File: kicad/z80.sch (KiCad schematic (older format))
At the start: 18 parts, among them J3 Conn_02x20_Odd_Even, U1 Z80CPU, U23 74AC273, U3 SST39SF010, U4 74AHC32, U5 AS6C1008-55PCN, U6 74HC154, U9 74AHC02, X1 ACH10MHZ

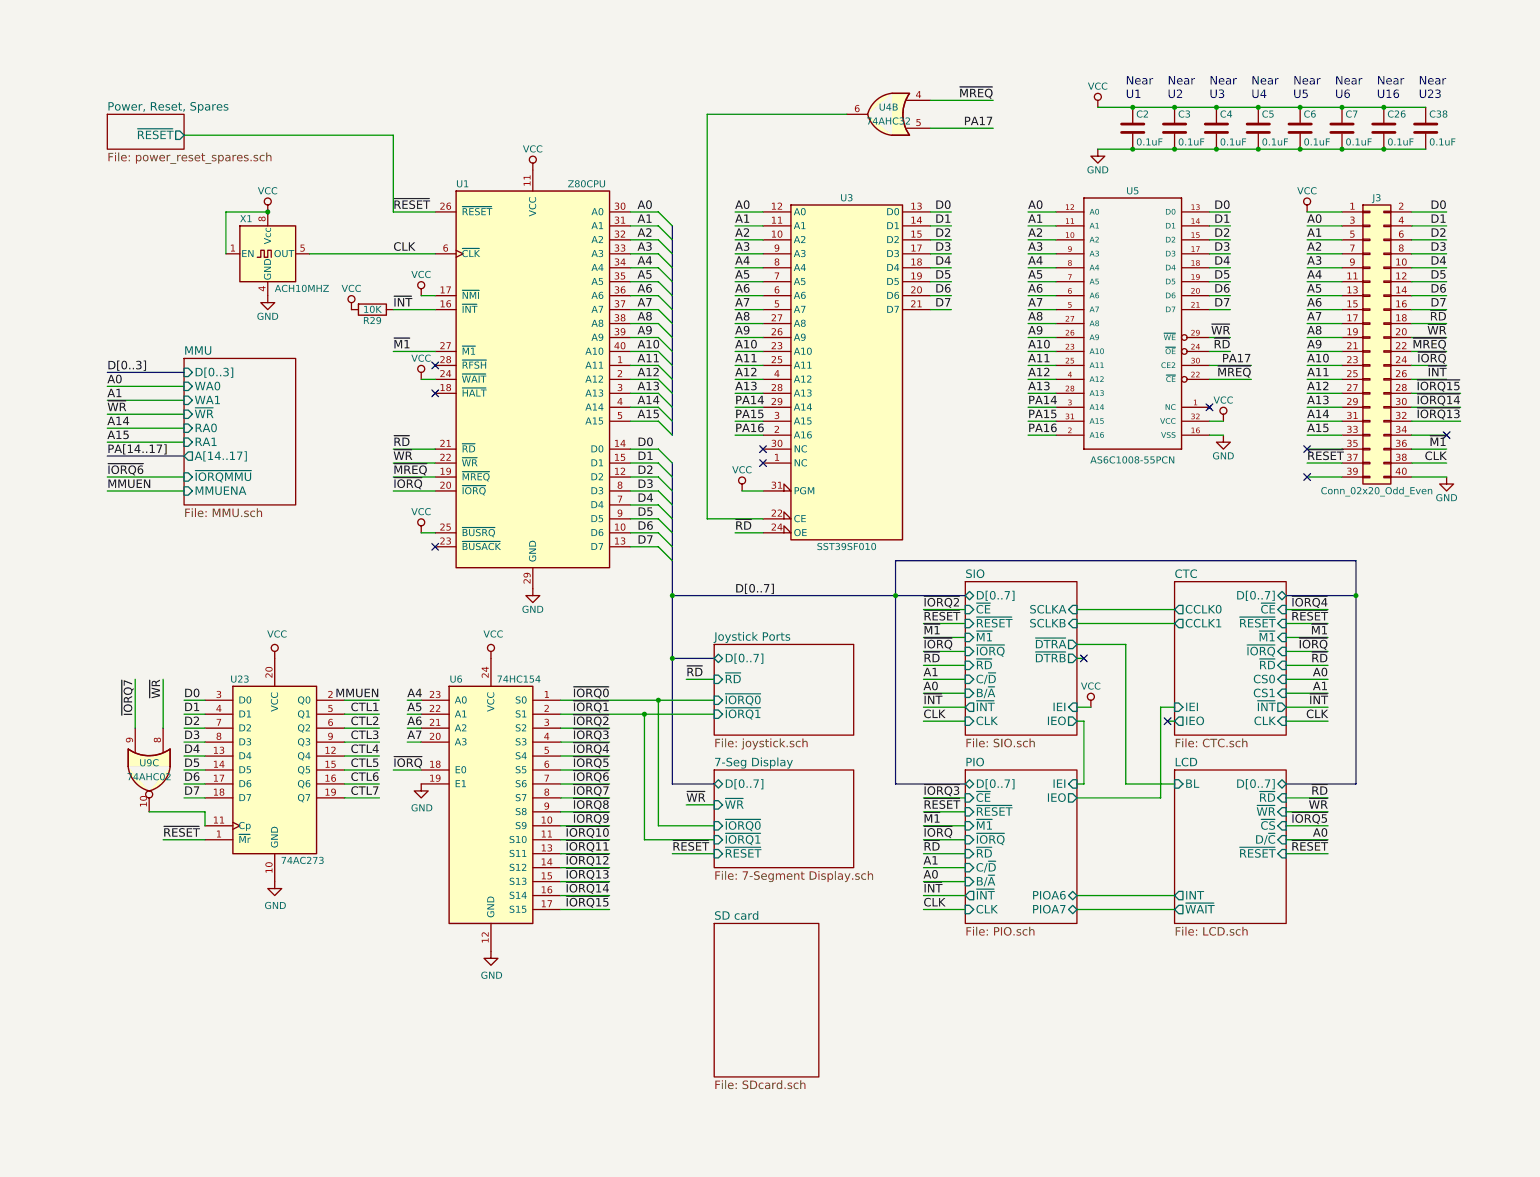
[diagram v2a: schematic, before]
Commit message: SDcard interface mostly complete.
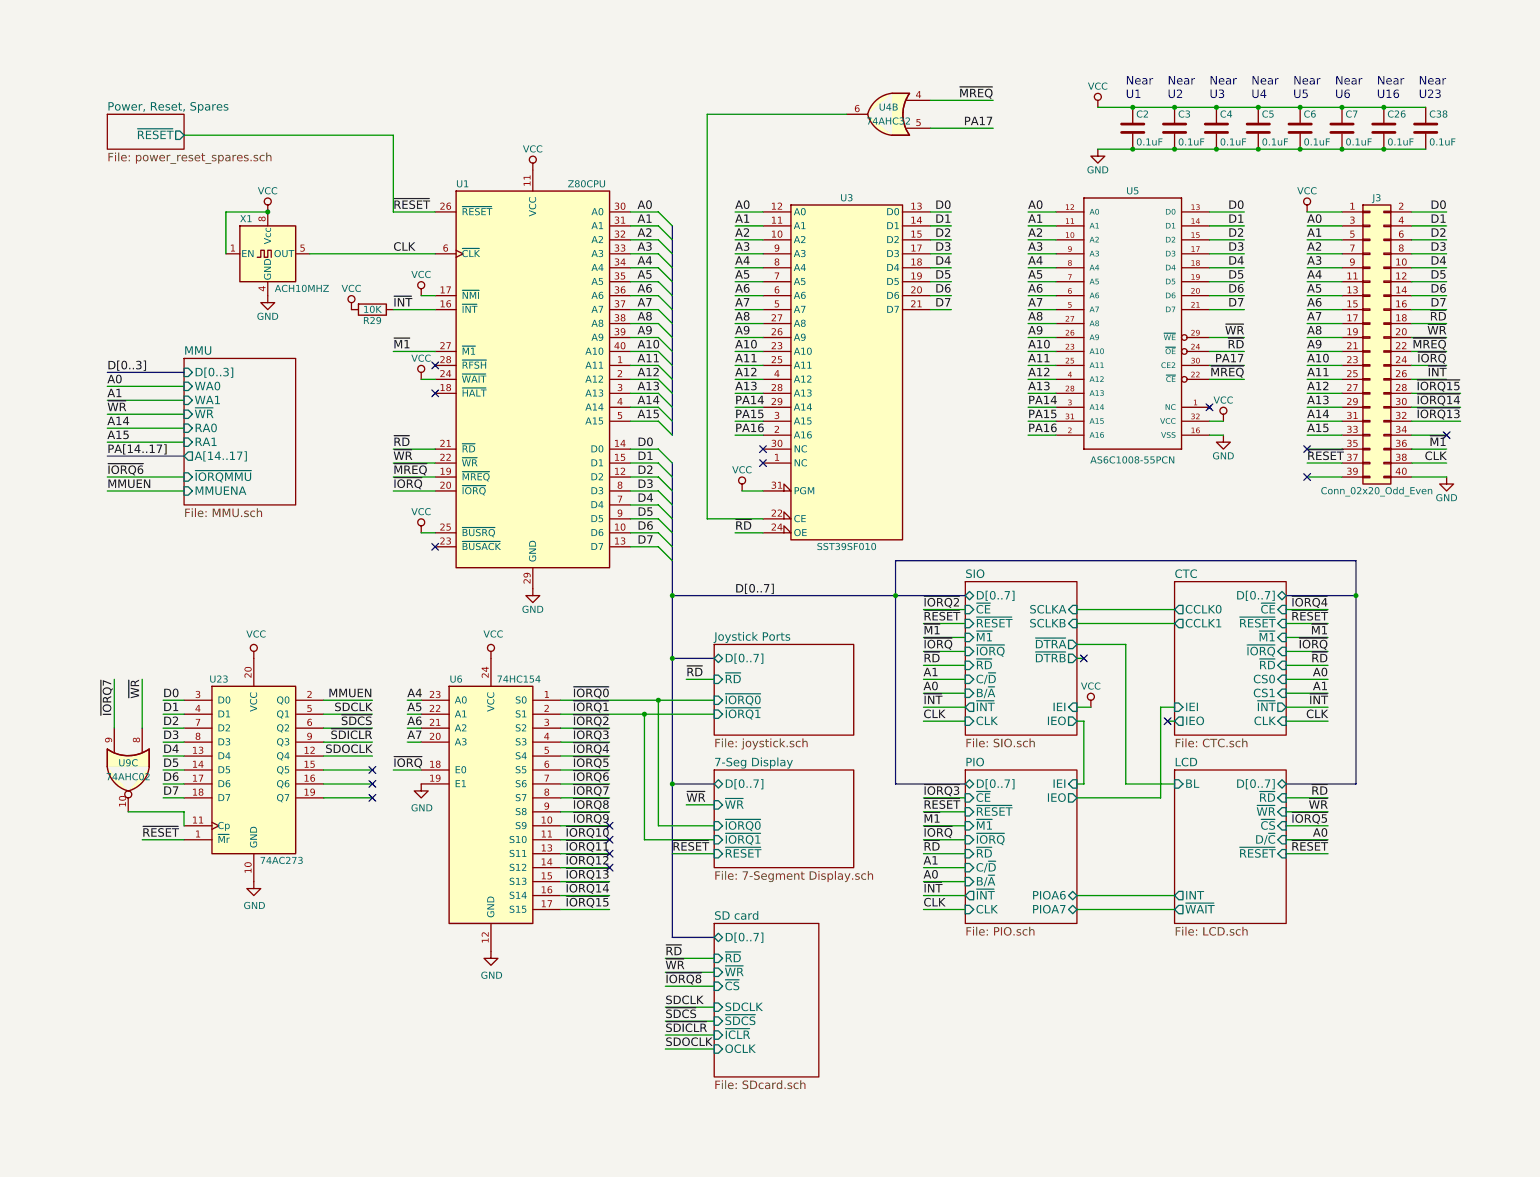
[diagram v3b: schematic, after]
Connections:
- net CTL1 renamed SDCLK
- net CTL2 renamed ~SDCS
- net CTL3 renamed ~SDICLR
- net CTL4 renamed SDOCLK
- net CTL5: no longer names the net of U23.15 (Q5)
- net CTL6: no longer names the net of U23.16 (Q6)
- net CTL7: no longer names the net of U23.19 (Q7)
- no-connect marks 11 -> 18
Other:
- moved on the sheet: U23, U9C
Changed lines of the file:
@@
 	1    0    0    -1
 $EndComp
-Text Label 8750 1550 2    60   ~ 0
+Text Label 8850 1550 2    60   ~ 0
 D0
-Text Label 8750 1650 2    60   ~ 0
+Text Label 8850 1650 2    60   ~ 0
 D1
-Text Label 8750 1750 2    60   ~ 0
+Text Label 8850 1750 2    60   ~ 0
 D2
-Text Label 8750 1850 2    60   ~ 0
+Text Label 8850 1850 2    60   ~ 0
 D3
-Text Label 8750 1950 2    60   ~ 0
+Text Label 8850 1950 2    60   ~ 0
 D4
-Text Label 8750 2050 2    60   ~ 0
+Text Label 8850 2050 2    60   ~ 0
 D5
-Text Label 8750 2150 2    60   ~ 0
+Text Label 8850 2150 2    60   ~ 0
 D6
-Text Label 8750 2250 2    60   ~ 0
+Text Label 8850 2250 2    60   ~ 0
 D7
 Text Label 7300 1550 0    60   ~ 0
@@
 Text Label 5200 3050 0    60   ~ 0
 PA15
-Text Label 8750 2450 2    60   ~ 0
+Text Label 8850 2450 2    60   ~ 0
 ~WR
-Text Label 8750 2550 2    60   ~ 0
+Text Label 8850 2550 2    60   ~ 0
 ~RD
 NoConn ~ 8600 2950
@@
 Text Notes 9200 750  0    60   ~ 0
 Near\nU5
-Text Label 8900 2750 2    60   ~ 0
+Text Label 8850 2750 2    60   ~ 0
 ~MREQ
 Text Label 2750 5550 0    60   ~ 0
@@
 Text Label 700  3450 0    60   ~ 0
 ~IORQ6
-Text Label 900  4900 3    60   ~ 0
+Text Label 750  4900 3    60   ~ 0
 ~IORQ7
 Text Label 700  3300 0    60   ~ 0
@@
 	7500 3150 7300 3150
 Wire Wire Line
-	8600 1550 8750 1550
-Wire Wire Line
-	8600 1650 8750 1650
-Wire Wire Line
-	8600 1750 8750 1750
-Wire Wire Line
-	8600 1850 8750 1850
-Wire Wire Line
-	8600 1950 8750 1950
-Wire Wire Line
-	8600 2050 8750 2050
-Wire Wire Line
-	8600 2150 8750 2150
-Wire Wire Line
-	8600 2250 8750 2250
-Wire Wire Line
 	7500 1550 7300 1550
 Wire Wire Line
@@
 Wire Wire Line
 	5400 3050 5200 3050
-Wire Wire Line
-	8600 2550 8750 2550
-Wire Wire Line
-	8600 2450 8750 2450
 Connection ~ 8950 800
 Connection ~ 8950 1100
-Wire Wire Line
-	8600 2750 8900 2750
-Wire Wire Line
-	8600 2650 8900 2650
 Connection ~ 9250 800
 Connection ~ 9250 1100
@@
 	700  3450 1250 3450
 Wire Wire Line
-	900  4900 900  5250
+	750  4900 750  5250
 Wire Bus Line
 	1250 2700 700  2700
@@
 Text Label 7300 3150 0    60   ~ 0
 PA16
-Text Label 8900 2650 2    60   ~ 0
+Text Label 8850 2650 2    60   ~ 0
 PA17
 Text Label 7050 950  2    60   ~ 0
@@
 F0 "SD card" 60
 F1 "SDcard.sch" 60
+F2 "D[0..7]" B L 5050 6750 60
+F3 "~RD" I L 5050 6900 60
+F4 "~WR" I L 5050 7000 60
+F5 "~CS" I L 5050 7100 60
+F6 "SDCLK" I L 5050 7250 60
+F7 "~SDCS" I L 5050 7350 60
+F8 "OCLK" I L 5050 7550 60
+F9 "~ICLR" I L 5050 7450 60
 $EndSheet
 $Comp
 L 74xx:74LS273 U23
 U 1 1 5C3D0091
-P 1900 5550
-F 0 "U23" H 1650 6200 50  0000 C CNN
-F 1 "74AC273" H 2100 4900 50  0000 C CNN
-F 2 "" H 1900 5550 50  0001 C CNN
-F 3 "http://www.ti.com/lit/gpn/sn74LS273" H 1900 5550 50  0001 C CNN
-	1    1900 5550
-	1    0    0    -1
-$EndComp
-Text Label 1100 6050 0    60   ~ 0
+P 1750 5550
+F 0 "U23" H 1500 6200 50  0000 C CNN
+F 1 "74AC273" H 1950 4900 50  0000 C CNN
+F 2 "" H 1750 5550 50  0001 C CNN
+F 3 "http://www.ti.com/lit/gpn/sn74LS273" H 1750 5550 50  0001 C CNN
+	1    1750 5550
+	1    0    0    -1
+$EndComp
+Text Label 950  6050 0    60   ~ 0
 ~RESET
-Text Label 1250 5050 0    60   ~ 0
+Text Label 1100 5050 0    60   ~ 0
 D0
-Text Label 1250 5150 0    60   ~ 0
+Text Label 1100 5150 0    60   ~ 0
 D1
-Text Label 1250 5250 0    60   ~ 0
+Text Label 1100 5250 0    60   ~ 0
 D2
-Text Label 1250 5350 0    60   ~ 0
+Text Label 1100 5350 0    60   ~ 0
 D3
-Text Label 1250 5450 0    60   ~ 0
+Text Label 1100 5450 0    60   ~ 0
 D4
-Text Label 1250 5550 0    60   ~ 0
+Text Label 1100 5550 0    60   ~ 0
 D5
-Text Label 1250 5650 0    60   ~ 0
+Text Label 1100 5650 0    60   ~ 0
 D6
-Text Label 1250 5750 0    60   ~ 0
+Text Label 1100 5750 0    60   ~ 0
 D7
 Wire Wire Line
-	1400 5050 1250 5050
-Wire Wire Line
-	1400 5150 1250 5150
-Wire Wire Line
-	1400 5250 1250 5250
-Wire Wire Line
-	1400 5350 1250 5350
-Wire Wire Line
-	1400 5450 1250 5450
-Wire Wire Line
-	1400 5550 1250 5550
-Wire Wire Line
-	1400 5650 1250 5650
-Wire Wire Line
-	1400 5750 1250 5750
-Wire Wire Line
-	1100 6050 1400 6050
-Wire Wire Line
-	2400 5050 2650 5050
-Wire Wire Line
-	2400 5150 2650 5150
-Wire Wire Line
-	2400 5250 2650 5250
-Wire Wire Line
-	2400 5350 2650 5350
-Wire Wire Line
-	2400 5450 2650 5450
-Wire Wire Line
-	2400 5550 2650 5550
-Wire Wire Line
-	2400 5650 2650 5650
-Wire Wire Line
-	2400 5750 2650 5750
-Text Label 2650 5050 2    60   ~ 0
+	1250 5050 1100 5050
+Wire Wire Line
+	1250 5150 1100 5150
+Wire Wire Line
+	1250 5250 1100 5250
+Wire Wire Line
+	1250 5350 1100 5350
+Wire Wire Line
+	1250 5450 1100 5450
+Wire Wire Line
+	1250 5550 1100 5550
+Wire Wire Line
+	1250 5650 1100 5650
+Wire Wire Line
+	1250 5750 1100 5750
+Wire Wire Line
+	950  6050 1250 6050
+Text Label 2600 5050 2    60   ~ 0
 MMUEN
-Text Label 2650 5150 2    60   ~ 0
-CTL1
-Text Label 2650 5250 2    60   ~ 0
-CTL2
-Text Label 2650 5350 2    60   ~ 0
-CTL3
-Text Label 2650 5450 2    60   ~ 0
-CTL4
-Text Label 2650 5550 2    60   ~ 0
-CTL5
-Text Label 2650 5650 2    60   ~ 0
-CTL6
-Text Label 2650 5750 2    60   ~ 0
-CTL7
+Text Label 2600 5150 2    60   ~ 0
+SDCLK
+Text Label 2600 5250 2    60   ~ 0
+~SDCS
+Text Label 2600 5350 2    60   ~ 0
+~SDICLR
+Text Label 2600 5450 2    60   ~ 0
+SDOCLK
 $Comp
 L 74xx:74HC02 U9
 U 3 1 5C48A0C2
-P 1000 5550
+P 850 5550
 AR Path="/5C48A0C2" Ref="U9"  Part="3"
 AR Path="/5B502B1D/5C48A0C2" Ref="U?"  Part="3"
-F 0 "U9" V 950 5550 50  0000 C CNN
-F 1 "74AHC02" V 1050 5550 50  0000 C CNN
-F 2 "Housings_DIP:DIP-14_W7.62mm_LongPads" H 1000 5550 50  0001 C CNN
-F 3 "" H 1000 5550 50  0001 C CNN
-	3    1000 5550
+F 0 "U9" V 800 5550 50  0000 C CNN
+F 1 "74AHC02" V 900 5550 50  0000 C CNN
+F 2 "Housings_DIP:DIP-14_W7.62mm_LongPads" H 850 5550 50  0001 C CNN
+F 3 "" H 850 5550 50  0001 C CNN
+	3    850  5550
 	0    1    1    0
 $EndComp
@@
 L power:GND #PWR098
 U 1 1 5C4ED809
-P 1900 6350
-F 0 "#PWR098" H 1900 6100 50  0001 C CNN
-F 1 "GND" H 1905 6177 50  0000 C CNN
-F 2 "" H 1900 6350 50  0001 C CNN
-F 3 "" H 1900 6350 50  0001 C CNN
-	1    1900 6350
+P 1750 6350
+F 0 "#PWR098" H 1750 6100 50  0001 C CNN
+F 1 "GND" H 1755 6177 50  0000 C CNN
+F 2 "" H 1750 6350 50  0001 C CNN
+F 3 "" H 1750 6350 50  0001 C CNN
+	1    1750 6350
 	1    0    0    -1
 $EndComp
@@
 L power:VCC #PWR097
 U 1 1 5C4EDEE4
-P 1900 4750
-F 0 "#PWR097" H 1900 4600 50  0001 C CNN
-F 1 "VCC" H 1917 4923 50  0000 C CNN
-F 2 "" H 1900 4750 50  0001 C CNN
-F 3 "" H 1900 4750 50  0001 C CNN
-	1    1900 4750
-	1    0    0    -1
-$EndComp
-Wire Wire Line
-	1400 5950 1400 5850
-Wire Wire Line
-	1400 5850 1000 5850
-Wire Wire Line
-	1100 5250 1100 4900
-Text Label 1100 4900 3    60   ~ 0
+P 1750 4750
+F 0 "#PWR097" H 1750 4600 50  0001 C CNN
+F 1 "VCC" H 1767 4923 50  0000 C CNN
+F 2 "" H 1750 4750 50  0001 C CNN
+F 3 "" H 1750 4750 50  0001 C CNN
+	1    1750 4750
+	1    0    0    -1
+$EndComp
+Wire Wire Line
+	1250 5950 1250 5850
+Wire Wire Line
+	1250 5850 850  5850
+Wire Wire Line
+	950  5250 950  4900
+Text Label 950  4900 3    60   ~ 0
 ~WR
 $Sheet
@@
 	4750 6150 5050 6150
 Wire Bus Line
+	4750 5650 4750 6750
+Wire Bus Line
+	4750 6750 5050 6750
+Connection ~ 4750 5650
+Text Label 4700 6900 0    60   ~ 0
+~RD
+Text Label 4700 7000 0    60   ~ 0
+~WR
+Text Label 4700 7100 0    60   ~ 0
+~IORQ8
+Text Label 4700 7250 0    60   ~ 0
+SDCLK
+Text Label 4700 7350 0    60   ~ 0
+~SDCS
+Text Label 4700 7450 0    60   ~ 0
+~SDICLR
+Text Label 4700 7550 0    60   ~ 0
+SDOCLK
+Wire Wire Line
+	4700 6900 5050 6900
+Wire Wire Line
+	4700 7000 5050 7000
+Wire Wire Line
+	4700 7100 5050 7100
+Wire Wire Line
+	4700 7250 5050 7250
+Wire Wire Line
+	4700 7350 5050 7350
+Wire Wire Line
+	4700 7450 5050 7450
+Wire Wire Line
+	4700 7550 5050 7550
+Wire Wire Line
+	8600 2650 8850 2650
+Wire Wire Line
+	8600 2750 8850 2750
+Wire Wire Line
+	8600 1550 8850 1550
+Wire Wire Line
+	8600 1650 8850 1650
+Wire Wire Line
+	8600 1750 8850 1750
+Wire Wire Line
+	8600 1850 8850 1850
+Wire Wire Line
+	8600 1950 8850 1950
+Wire Wire Line
+	8600 2050 8850 2050
+Wire Wire Line
+	8600 2150 8850 2150
+Wire Wire Line
+	8600 2250 8850 2250
+Wire Wire Line
+	8600 2450 8850 2450
+Wire Wire Line
+	8600 2550 8850 2550
+Wire Wire Line
+	2250 5050 2600 5050
+NoConn ~ 2600 5550
+Wire Wire Line
+	2250 5150 2600 5150
+Wire Wire Line
+	2250 5250 2600 5250
+Wire Wire Line
+	2250 5350 2600 5350
+Wire Wire Line
+	2250 5450 2600 5450
+Wire Wire Line
+	2250 5550 2600 5550
+Wire Wire Line
+	2250 5650 2600 5650
+Wire Wire Line
+	2250 5750 2600 5750
+NoConn ~ 2600 5650
+NoConn ~ 2600 5750
+NoConn ~ 4300 5950
+NoConn ~ 4300 6050
+NoConn ~ 4300 6150
+NoConn ~ 4300 6250
+Wire Bus Line
 	4750 3350 4750 4300

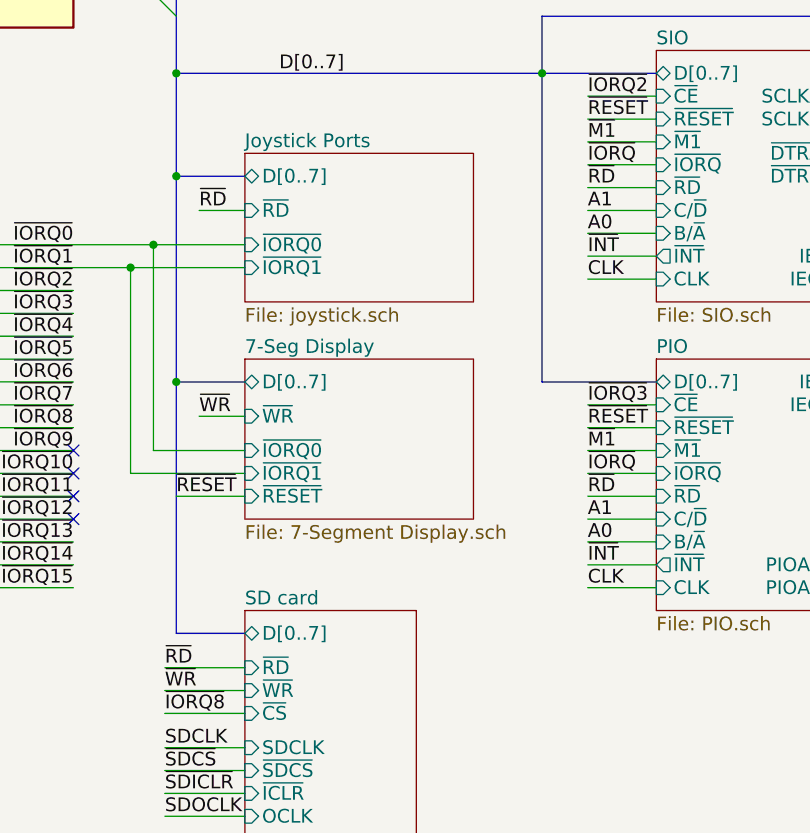
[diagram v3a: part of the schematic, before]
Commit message: Hook up SD card slot's write protect and card detect lines.
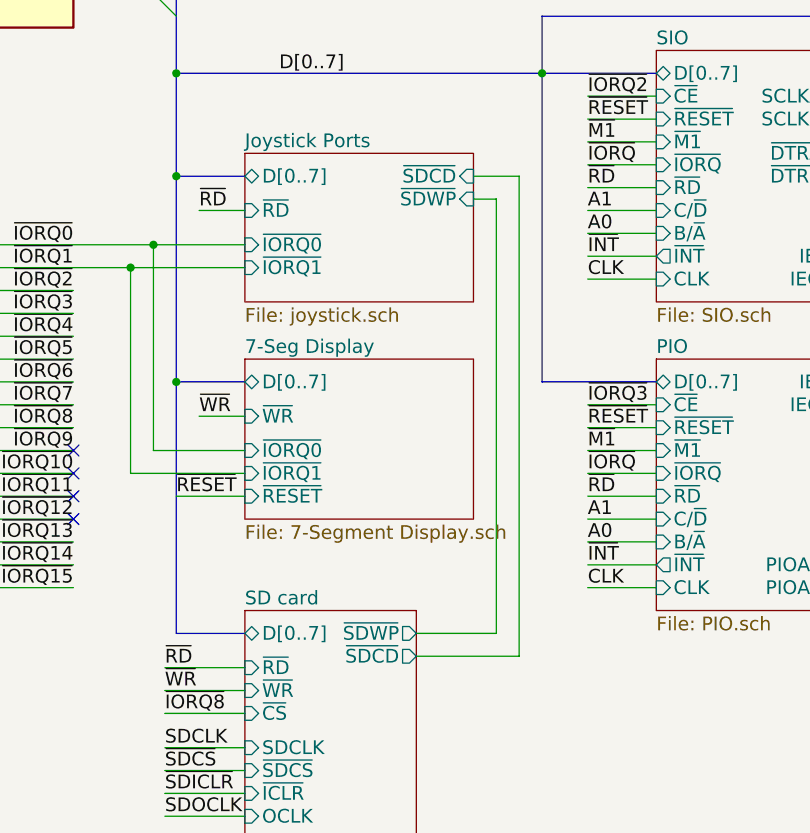
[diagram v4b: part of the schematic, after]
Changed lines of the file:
@@
 F4 "~IORQ1" I L 5050 5150 60
 F5 "D[0..7]" B L 5050 4750 60
+F6 "~SDCD" I R 6050 4750 60
+F7 "~SDWP" I R 6050 4850 60
 $EndSheet
 Text Label 4300 5350 2    60   ~ 0
@@
 F8 "OCLK" I L 5050 7550 60
 F9 "~ICLR" I L 5050 7450 60
+F10 "~SDWP" O R 5800 6750 60
+F11 "~SDCD" O R 5800 6850 60
 $EndSheet
 $Comp
@@
 NoConn ~ 4300 6150
 NoConn ~ 4300 6250
+Wire Wire Line
+	6050 4850 6150 4850
+Wire Wire Line
+	6150 4850 6150 6750
+Wire Wire Line
+	6150 6750 5800 6750
+Wire Wire Line
+	5800 6850 6250 6850
+Wire Wire Line
+	6250 6850 6250 4750
+Wire Wire Line
+	6250 4750 6050 4750
 Wire Bus Line
 	4750 3350 4750 4300
